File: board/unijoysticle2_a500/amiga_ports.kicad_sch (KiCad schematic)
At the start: 23 parts

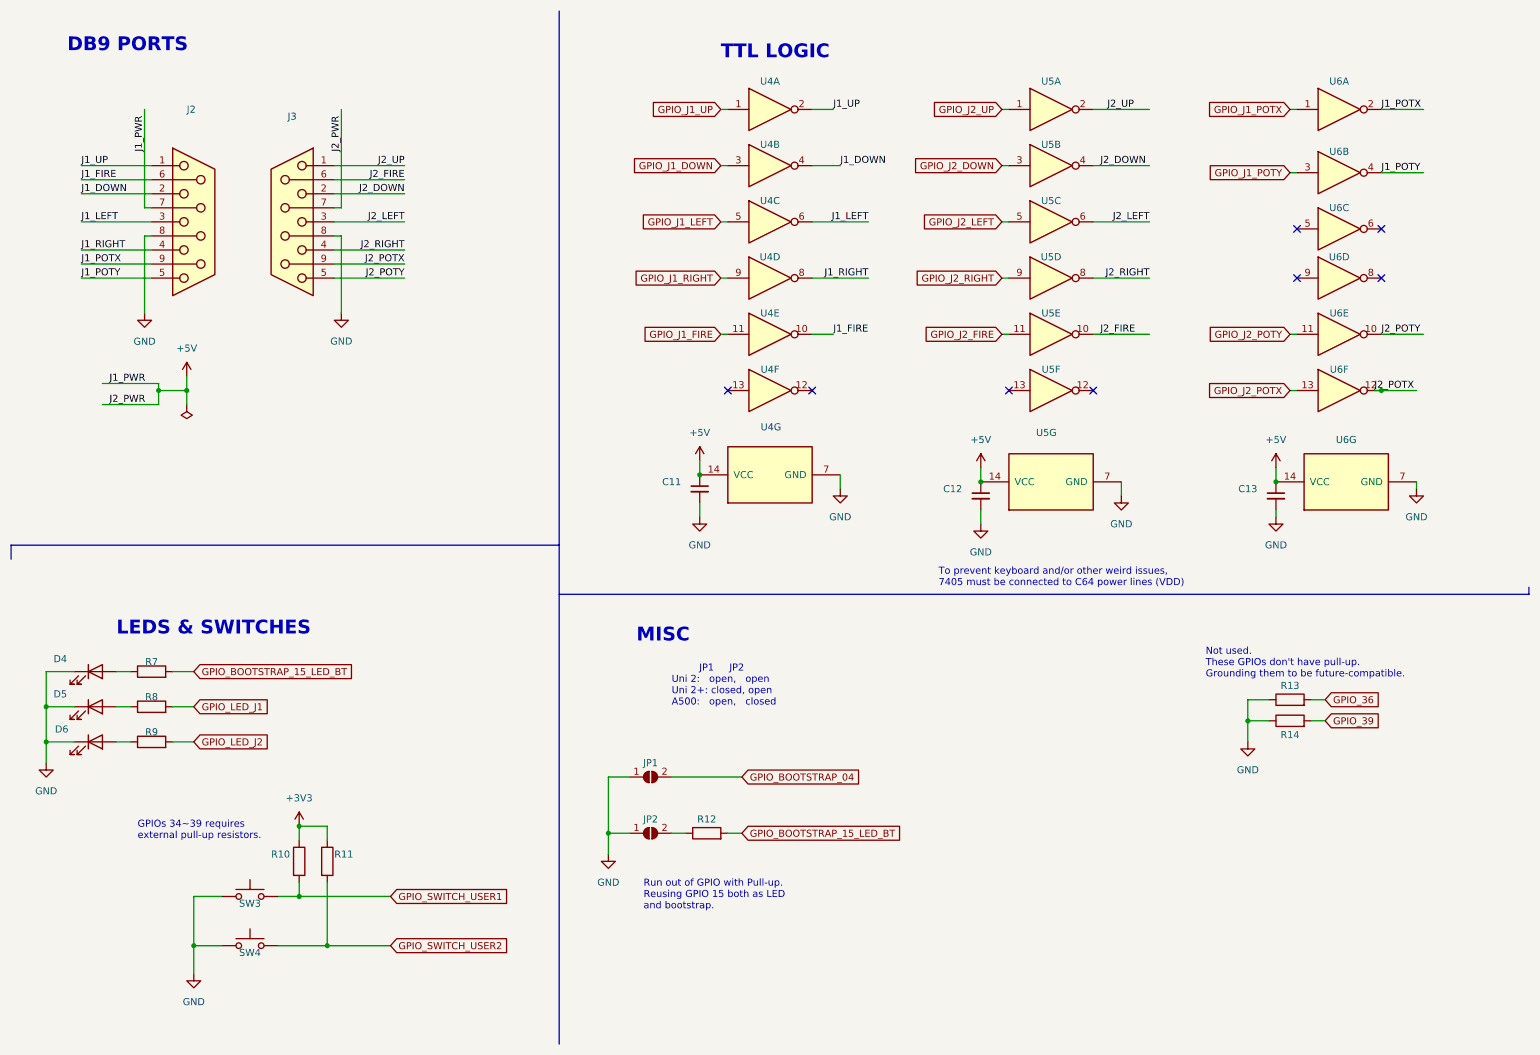
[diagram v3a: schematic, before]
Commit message: Uni 2 A500 Rev B:
- Cap 1500uF instead of 1000uF
- Use Resister 0 (R15) instead of JP2. Back resistor for JP2 2.2K
- LED resistors to be 2.2K
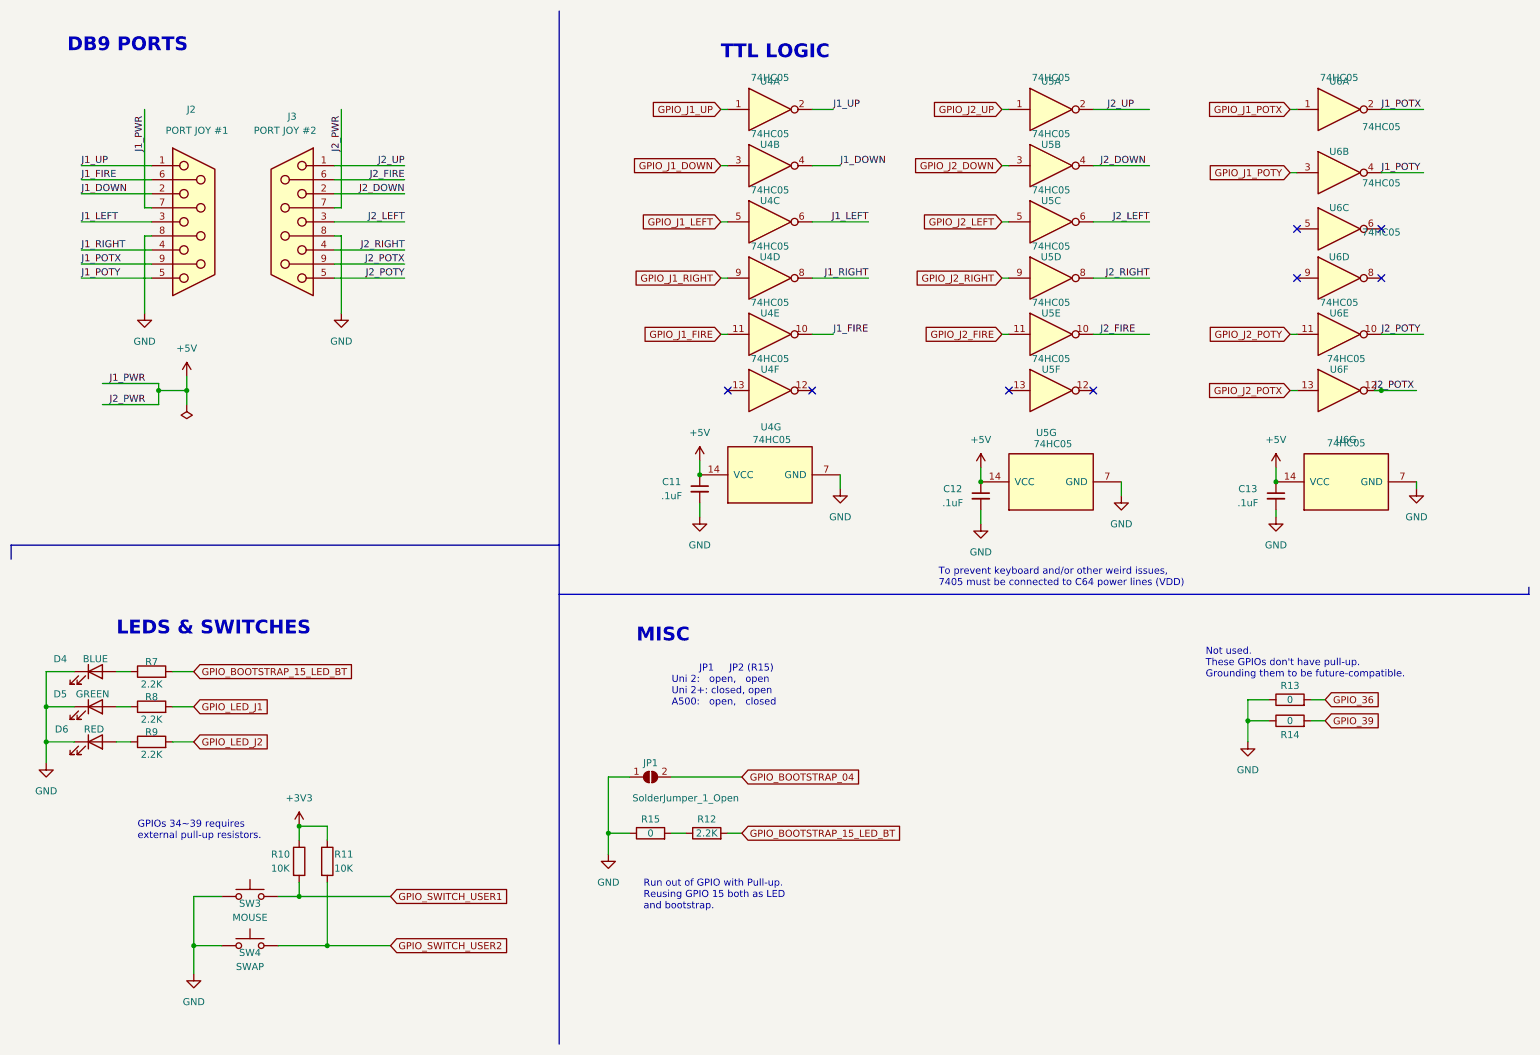
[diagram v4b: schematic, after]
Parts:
- removed JP2: (no value), symbol Jumper:SolderJumper_2_Open
- added R15: 0, Resistor_SMD:R_0805_2012Metric_Pad1.20x1.40mm_HandSolder, symbol Device:R
- C11, C12, C13: value (none) -> .1uF; footprint (none) -> Capacitor_SMD:C_0805_2012Metric_Pad1.18x1.45mm_HandSolder
- D4: value (none) -> BLUE; footprint (none) -> LED_SMD:LED_0805_2012Metric_Pad1.15x1.40mm_HandSolder
- D5: value (none) -> GREEN; footprint (none) -> LED_SMD:LED_0805_2012Metric_Pad1.15x1.40mm_HandSolder
- D6: value (none) -> RED; footprint (none) -> LED_SMD:LED_0805_2012Metric_Pad1.15x1.40mm_HandSolder
- J2: value (none) -> PORT JOY #1; footprint (none) -> Connector_Dsub:DSUB-9_Female_Horizontal_P2.77x2.54mm_EdgePinOffset9.40mm
- J3: value (none) -> PORT JOY #2; footprint (none) -> Connector_Dsub:DSUB-9_Female_Horizontal_P2.77x2.54mm_EdgePinOffset9.40mm
- JP1: value (none) -> SolderJumper_1_Open; footprint (none) -> Jumper:SolderJumper-2_P1.3mm_Open_Pad1.0x1.5mm
- R10, R11: value (none) -> 10K; footprint (none) -> Resistor_SMD:R_0805_2012Metric_Pad1.20x1.40mm_HandSolder
- R12, R7, R8, R9: value (none) -> 2.2K; footprint (none) -> Resistor_SMD:R_0805_2012Metric_Pad1.20x1.40mm_HandSolder
- R13, R14: value (none) -> 0; footprint (none) -> Resistor_SMD:R_0805_2012Metric_Pad1.20x1.40mm_HandSolder
- SW3: value (none) -> MOUSE; footprint (none) -> Button_Switch_THT:SW_Tactile_SPST_Angled_PTS645Vx39-2LFS
- SW4: value (none) -> SWAP; footprint (none) -> Button_Switch_THT:SW_Tactile_SPST_Angled_PTS645Vx39-2LFS
- U4, U5, U6: value (none) -> 74HC05; footprint (none) -> Package_SO:SOIC-14_3.9x8.7mm_P1.27mm
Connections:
- net GND: now also R15.1
- net at R12.1: now also R15.2
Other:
- note added: "JP1 JP2 (R15) Uni 2: open, open Uni 2+: closed, open A500: open, closed"
- note removed: "JP1 JP2 Uni 2: open, open Uni 2+: closed, open A500: open, closed"

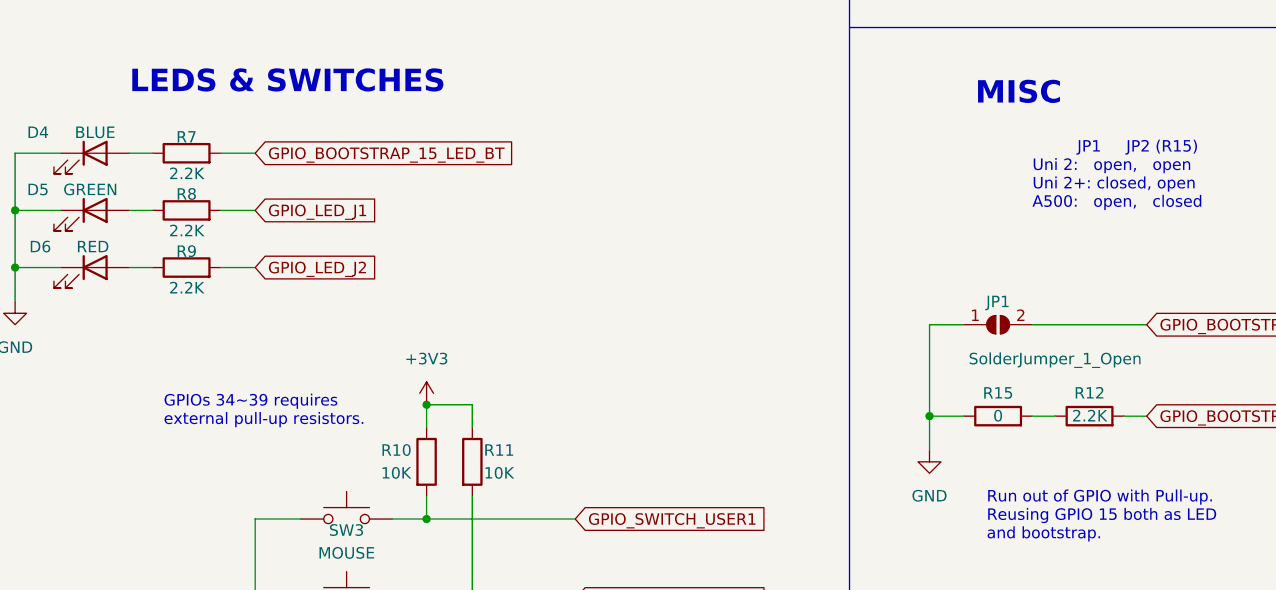
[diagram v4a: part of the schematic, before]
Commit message: uni2 a500: revert CH340 from 5V
Autoreset is driven by DTS/RTS.
But if DTS/RTS are not used (requires that CH340 is powered) then
autoreset doesn't work.
So, although we shouldn't power CH340 when it is powered from the Amiga,
since it consumes current, we need it for autoreset.

Besides, we don't gain much by not powering CH340. Only 0.02 amps
according to my measures.
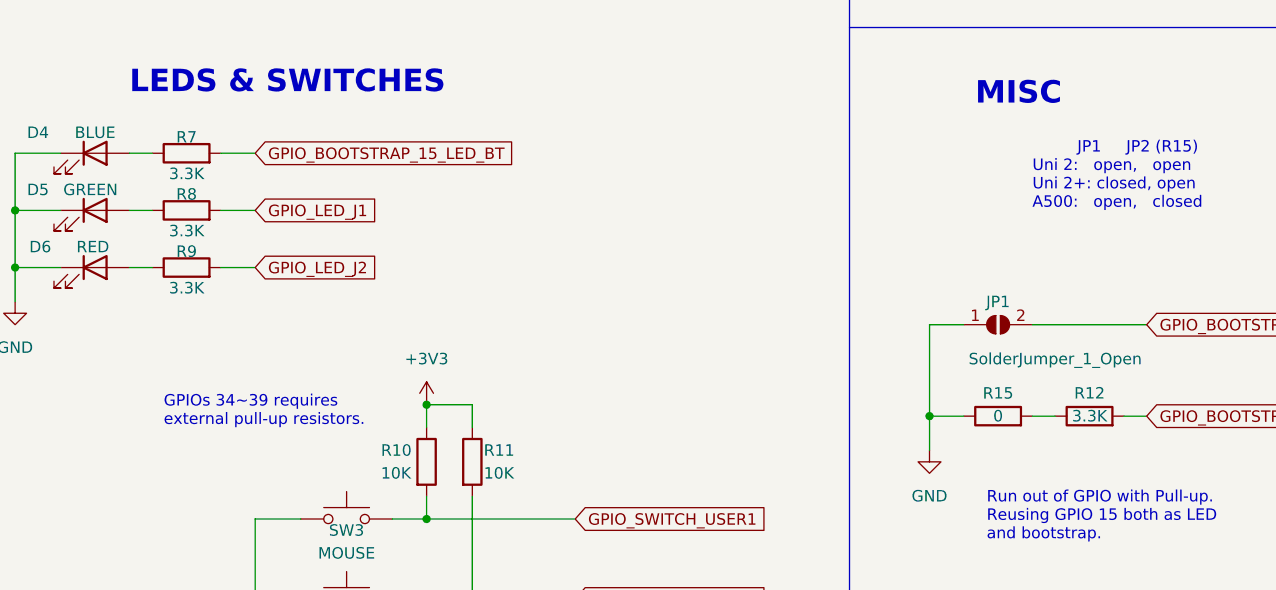
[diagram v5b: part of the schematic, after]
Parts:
- R12, R7, R8, R9: value 2.2K -> 3.3K
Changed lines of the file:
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@@
   (title_block
     (title "Unijoysticle 2 A500")
-    (date "2022-05-15")
-    (rev "B")
+    (date "2022-05-26")
+    (rev "C")
     (company "Retro Moe")
   )
@@
     (in_bom yes) (on_board yes)
     (property "Reference" "R8" (id 0) (at 36.83 136.652 90))
-    (property "Value" "2.2K" (id 1) (at 36.83 140.716 90))
+    (property "Value" "3.3K" (id 1) (at 36.83 140.716 90))
     (property "Footprint" "Resistor_SMD:R_0805_2012Metric_Pad1.20x1.40mm_HandSolder" (id 2) (at 36.83 140.208 90)
       (effects (font (size 1.27 1.27)) hide)
@@
     (in_bom yes) (on_board yes)
     (property "Reference" "R7" (id 0) (at 36.83 130.302 90))
-    (property "Value" "2.2K" (id 1) (at 36.83 134.366 90))
+    (property "Value" "3.3K" (id 1) (at 36.83 134.366 90))
     (property "Footprint" "Resistor_SMD:R_0805_2012Metric_Pad1.20x1.40mm_HandSolder" (id 2) (at 36.83 133.858 90)
       (effects (font (size 1.27 1.27)) hide)
@@
     (in_bom yes) (on_board yes)
     (property "Reference" "R9" (id 0) (at 36.83 143.002 90))
-    (property "Value" "2.2K" (id 1) (at 36.83 147.066 90))
+    (property "Value" "3.3K" (id 1) (at 36.83 147.066 90))
     (property "Footprint" "Resistor_SMD:R_0805_2012Metric_Pad1.20x1.40mm_HandSolder" (id 2) (at 36.83 146.558 90)
       (effects (font (size 1.27 1.27)) hide)
@@
     (in_bom yes) (on_board yes)
     (property "Reference" "R12" (id 0) (at 137.16 158.75 90))
-    (property "Value" "2.2K" (id 1) (at 137.16 161.29 90))
+    (property "Value" "3.3K" (id 1) (at 137.16 161.29 90))
     (property "Footprint" "Resistor_SMD:R_0805_2012Metric_Pad1.20x1.40mm_HandSolder" (id 2) (at 137.16 163.068 90)
       (effects (font (size 1.27 1.27)) hide)

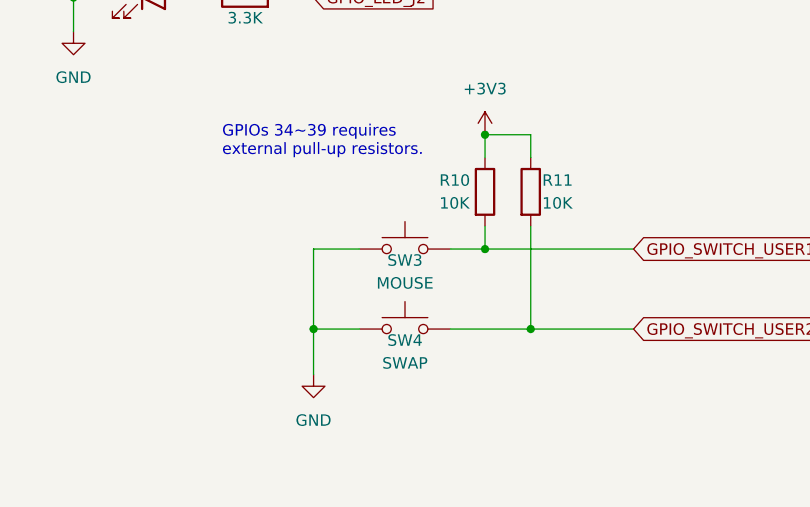
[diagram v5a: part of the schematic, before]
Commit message: uni2 a500: silkscreen improments
mouse -> mode
add copyright
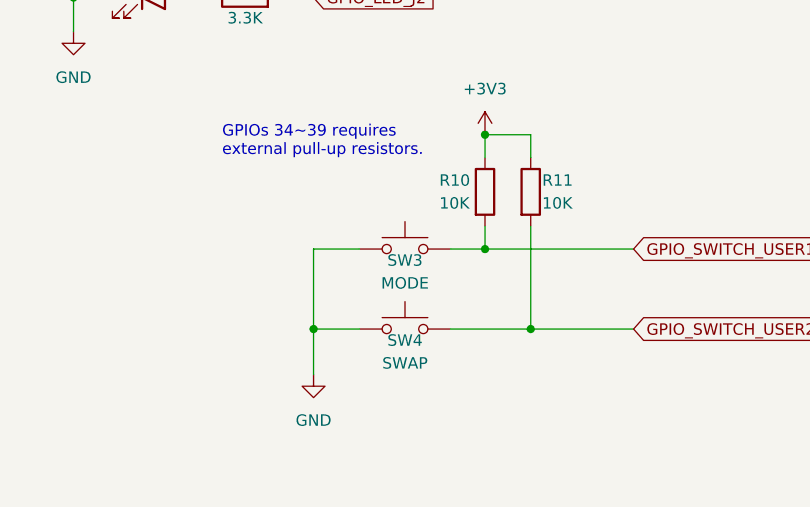
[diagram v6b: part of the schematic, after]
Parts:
- SW3: value MOUSE -> MODE
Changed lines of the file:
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@@
     (in_bom yes) (on_board yes)
     (property "Reference" "SW3" (id 0) (at 54.61 173.99 0))
-    (property "Value" "MOUSE" (id 1) (at 54.61 176.53 0))
+    (property "Value" "MODE" (id 1) (at 54.61 176.53 0))
     (property "Footprint" "Button_Switch_THT:SW_Tactile_SPST_Angled_PTS645Vx39-2LFS" (id 2) (at 54.61 167.64 0)
       (effects (font (size 1.27 1.27)) hide)

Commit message: Uni2 A500: Change company name
from Retro Moe to Ricardo Quesada
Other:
- company: Retro Moe -> Ricardo Quesada
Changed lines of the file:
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@@
     (date "2022-05-26")
     (rev "C")
-    (company "Retro Moe")
+    (company "Ricardo Quesada")
   )
   (junction (at 17.78 144.78) (diameter 0) (color 0 0 0 0)
